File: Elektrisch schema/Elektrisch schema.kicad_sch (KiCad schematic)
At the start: 5 parts, among them J1 Conn_01x03_Socket, Q1 NPN

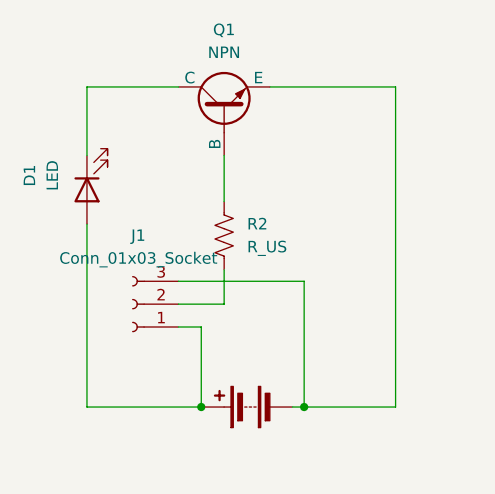
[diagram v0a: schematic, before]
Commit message: elektisch shema second draft
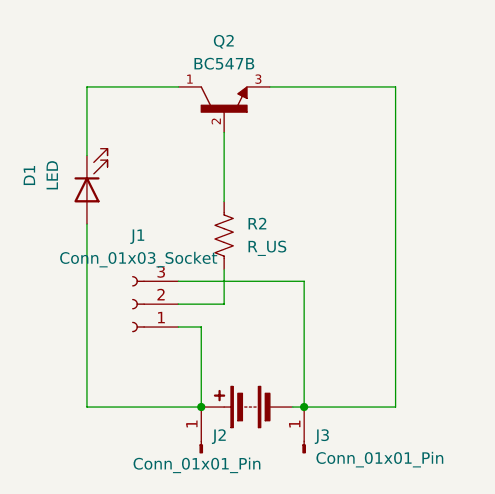
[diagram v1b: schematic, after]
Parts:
- removed Q1: NPN, symbol Simulation_SPICE:NPN
- added J2, J3: Conn_01x01_Pin, Connector_PinHeader_2.54mm:PinHeader_1x01_P2.54mm_Vertical, symbol Connector:Conn_01x01_Pin
- added Q2: BC547B, BC547B:TO92250P510H770-3, symbol BC547B:BC547B
- J1: footprint (none) -> Connector_PinHeader_2.54mm:PinHeader_1x03_P2.54mm_Vertical
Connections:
- net at D1.1 (K): now also Q2.1
- net at BT1.1 (+), D1.2 (A), J1.1 (Pin_1): now also J2.1 (Pin_1)
- net at BT1.2 (-), J1.3 (Pin_3): now also J3.1 (Pin_1), Q2.3
- net at R2.1: now also Q2.2
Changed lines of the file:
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@@
     (stroke (width 0) (type default))
   )
-  (wire (pts (xy 113.03 76.2) (xy 113.03 81.28))
+  (wire (pts (xy 113.03 73.66) (xy 113.03 81.28))
     (stroke (width 0) (type default))
   )
@@
     )
   )
+  (symbol (lib_id "BC547B:BC547B") (at 113.03 71.12 90) (unit 1)
+    (in_bom yes) (on_board yes) (dnp no) (fields_autoplaced)
+    (property "Reference" "Q2" (at 113.03 63.5 90)
+      (effects (font (size 1.27 1.27)))
+    )
+    (property "Value" "BC547B" (at 113.03 66.04 90)
+      (effects (font (size 1.27 1.27)))
+    )
+    (property "Footprint" "BC547B:TO92250P510H770-3" (at 113.03 71.12 0)
+      (effects (font (size 1.27 1.27)) (justify bottom) hide)
+    )
+    (property "Datasheet" "" (at 113.03 71.12 0)
+      (effects (font (size 1.27 1.27)) hide)
+    )
+    (property "MF" "onsemi" (at 113.03 71.12 0)
+      (effects (font (size 1.27 1.27)) (justify bottom) hide)
+    )
+    (property "Purchase-URL" "https://www.snapeda.com/api/url_track_click_mouser/?unipart_id=7207558&manufacturer=onsemi&part_name=BC547B&search_term=None" (at 113.03 71.12 0)
+      (effects (font (size 1.27 1.27)) (justify bottom) hide)
+    )
+    (property "Package" "E-PKG AXIAL-LEADED-2 ON Semiconductor" (at 113.03 71.12 0)
+      (effects (font (size 1.27 1.27)) (justify bottom) hide)
+    )
+    (property "Price" "None" (at 113.03 71.12 0)
+      (effects (font (size 1.27 1.27)) (justify bottom) hide)
+    )
+    (property "Check_prices" "https://www.snapeda.com/parts/BC547B/Onsemi/view-part/?ref=eda" (at 113.03 71.12 0)
+      (effects (font (size 1.27 1.27)) (justify bottom) hide)
+    )
+    (property "SnapEDA_Link" "https://www.snapeda.com/parts/BC547B/Onsemi/view-part/?ref=snap" (at 113.03 71.12 0)
+      (effects (font (size 1.27 1.27)) (justify bottom) hide)
+    )
+    (property "MP" "BC547B" (at 113.03 71.12 0)
+      (effects (font (size 1.27 1.27)) (justify bottom) hide)
+    )
+    (property "Availability" "In Stock" (at 113.03 71.12 0)
+      (effects (font (size 1.27 1.27)) (justify bottom) hide)
+    )
+    (property "Description" "\nBipolar (BJT) Transistor NPN 45 V 100 mA 300MHz 500 mW Through Hole TO-92-3\n" (at 113.03 71.12 0)
+      (effects (font (size 1.27 1.27)) (justify bottom) hide)
+    )
+    (pin "1")
+    (pin "2")
+    (pin "3")
+    (instances
+      (project "Elektrisch schema"
+        (path "/85b27cc0-7b51-4c2c-b0d4-ad8ed33695ec"
+          (reference "Q2") (unit 1)
+        )
+      )
+    )
+  )
   (symbol (lib_id "Device:Battery") (at 115.57 104.14 90) (unit 1)
     (in_bom yes) (on_board yes) (dnp no) (fields_autoplaced)
@@
     )
   )
-  (symbol (lib_id "Simulation_SPICE:NPN") (at 113.03 71.12 90) (unit 1)
+  (symbol (lib_id "Connector:Conn_01x01_Pin") (at 121.92 109.22 90) (unit 1)
     (in_bom yes) (on_board yes) (dnp no) (fields_autoplaced)
-    (property "Reference" "Q1" (at 113.03 62.23 90)
-      (effects (font (size 1.27 1.27)))
+    (property "Reference" "J3" (at 123.19 107.315 90)
+      (effects (font (size 1.27 1.27)) (justify right))
     )
-    (property "Value" "NPN" (at 113.03 64.77 90)
-      (effects (font (size 1.27 1.27)))
+    (property "Value" "Conn_01x01_Pin" (at 123.19 109.855 90)
+      (effects (font (size 1.27 1.27)) (justify right))
     )
-    (property "Footprint" "" (at 113.03 7.62 0)
+    (property "Footprint" "Connector_PinHeader_2.54mm:PinHeader_1x01_P2.54mm_Vertical" (at 121.92 109.22 0)
       (effects (font (size 1.27 1.27)) hide)
     )
-    (property "Datasheet" "~" (at 113.03 7.62 0)
-      (effects (font (size 1.27 1.27)) hide)
-    )
-    (property "Sim.Device" "NPN" (at 113.03 71.12 0)
-      (effects (font (size 1.27 1.27)) hide)
-    )
-    (property "Sim.Type" "GUMMELPOON" (at 113.03 71.12 0)
-      (effects (font (size 1.27 1.27)) hide)
-    )
-    (property "Sim.Pins" "1=C 2=B 3=E" (at 113.03 71.12 0)
+    (property "Datasheet" "~" (at 121.92 109.22 0)
       (effects (font (size 1.27 1.27)) hide)
     )
     (pin "1")
-    (pin "2")
-    (pin "3")
     (instances
       (project "Elektrisch schema"
         (path "/85b27cc0-7b51-4c2c-b0d4-ad8ed33695ec"
-          (reference "Q1") (unit 1)
+          (reference "J3") (unit 1)
+        )
+      )
+    )
+  )
+  (symbol (lib_id "Connector:Conn_01x01_Pin") (at 110.49 109.22 90) (unit 1)
+    (in_bom yes) (on_board yes) (dnp no)
+    (property "Reference" "J2" (at 111.76 107.315 90)
+      (effects (font (size 1.27 1.27)) (justify right))
+    )
+    (property "Value" "Conn_01x01_Pin" (at 102.87 110.49 90)
+      (effects (font (size 1.27 1.27)) (justify right))
+    )
+    (property "Footprint" "Connector_PinHeader_2.54mm:PinHeader_1x01_P2.54mm_Vertical" (at 110.49 109.22 0)
+      (effects (font (size 1.27 1.27)) hide)
+    )
+    (property "Datasheet" "~" (at 110.49 109.22 0)
+      (effects (font (size 1.27 1.27)) hide)
+    )
+    (pin "1")
+    (instances
+      (project "Elektrisch schema"
+        (path "/85b27cc0-7b51-4c2c-b0d4-ad8ed33695ec"
+          (reference "J2") (unit 1)
         )
       )
@@
       (effects (font (size 1.27 1.27)))
     )
-    (property "Footprint" "" (at 102.87 92.71 0)
+    (property "Footprint" "Connector_PinHeader_2.54mm:PinHeader_1x03_P2.54mm_Vertical" (at 102.87 92.71 0)
       (effects (font (size 1.27 1.27)) hide)
     )

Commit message: updating github
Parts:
- added D2: 1N4001, Diode_THT:D_DO-41_SOD81_P10.16mm_Horizontal, symbol Diode:1N4001
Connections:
- net at BT1.1 (+), D1.2 (A), J1.1 (Pin_1): now also D2.1 (K); no longer J2.1 (Pin_1)
- new net: D2.2 (A), J2.1 (Pin_1)
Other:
- moved on the sheet: J2
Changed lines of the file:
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@@
 (kicad_sch (version 20230121) (generator eeschema)
   (paper "A4")
+  (junction (at 110.49 104.14) (diameter 0) (color 0 0 0 0)
+  )
   (junction (at 121.92 104.14) (diameter 0) (color 0 0 0 0)
   )
-  (junction (at 110.49 104.14) (diameter 0) (color 0 0 0 0)
+  (junction (at 104.14 104.14) (diameter 0) (color 0 0 0 0)
   )
   (wire (pts (xy 121.92 90.17) (xy 121.92 104.14))
@@
     (stroke (width 0) (type default))
   )
-  (wire (pts (xy 110.49 104.14) (xy 97.79 104.14))
+  (wire (pts (xy 104.14 104.14) (xy 97.79 104.14))
     (stroke (width 0) (type default))
   )
@@
     (stroke (width 0) (type default))
   )
-  (wire (pts (xy 107.95 95.25) (xy 110.49 95.25))
+  (wire (pts (xy 104.14 95.25) (xy 107.95 95.25))
     (stroke (width 0) (type default))
   )
@@
     (stroke (width 0) (type default))
   )
-  (wire (pts (xy 110.49 95.25) (xy 110.49 104.14))
+  (wire (pts (xy 111.76 104.14) (xy 110.49 104.14))
+    (stroke (width 0) (type default))
+  )
+  (wire (pts (xy 104.14 95.25) (xy 104.14 104.14))
     (stroke (width 0) (type default))
   )
@@
   )
   (wire (pts (xy 121.92 104.14) (xy 132.08 104.14))
+    (stroke (width 0) (type default))
+  )
+  (wire (pts (xy 104.14 104.14) (xy 110.49 104.14))
+    (stroke (width 0) (type default))
+  )
+  (wire (pts (xy 111.76 106.68) (xy 111.76 104.14))
+    (stroke (width 0) (type default))
+  )
+  (wire (pts (xy 104.14 106.68) (xy 104.14 109.22))
     (stroke (width 0) (type default))
   )
@@
     )
   )
+  (symbol (lib_id "Diode:1N4001") (at 107.95 106.68 180) (unit 1)
+    (in_bom yes) (on_board yes) (dnp no) (fields_autoplaced)
+    (property "Reference" "D2" (at 107.95 113.03 0)
+      (effects (font (size 1.27 1.27)))
+    )
+    (property "Value" "1N4001" (at 107.95 110.49 0)
+      (effects (font (size 1.27 1.27)))
+    )
+    (property "Footprint" "Diode_THT:D_DO-41_SOD81_P10.16mm_Horizontal" (at 107.95 106.68 0)
+      (effects (font (size 1.27 1.27)) hide)
+    )
+    (property "Datasheet" "http://www.vishay.com/docs/88503/1n4001.pdf" (at 107.95 106.68 0)
+      (effects (font (size 1.27 1.27)) hide)
+    )
+    (property "Sim.Device" "D" (at 107.95 106.68 0)
+      (effects (font (size 1.27 1.27)) hide)
+    )
+    (property "Sim.Pins" "1=K 2=A" (at 107.95 106.68 0)
+      (effects (font (size 1.27 1.27)) hide)
+    )
+    (pin "1")
+    (pin "2")
+    (instances
+      (project "Elektrisch schema"
+        (path "/85b27cc0-7b51-4c2c-b0d4-ad8ed33695ec"
+          (reference "D2") (unit 1)
+        )
+      )
+    )
+  )
   (symbol (lib_id "Connector:Conn_01x01_Pin") (at 121.92 109.22 90) (unit 1)
     (in_bom yes) (on_board yes) (dnp no) (fields_autoplaced)
@@
     )
   )
-  (symbol (lib_id "Connector:Conn_01x01_Pin") (at 110.49 109.22 90) (unit 1)
+  (symbol (lib_id "Connector:Conn_01x01_Pin") (at 104.14 114.3 90) (unit 1)
     (in_bom yes) (on_board yes) (dnp no)
-    (property "Reference" "J2" (at 111.76 107.315 90)
-      (effects (font (size 1.27 1.27)) (justify right))
-    )
-    (property "Value" "Conn_01x01_Pin" (at 102.87 110.49 90)
-      (effects (font (size 1.27 1.27)) (justify right))
-    )
-    (property "Footprint" "Connector_PinHeader_2.54mm:PinHeader_1x01_P2.54mm_Vertical" (at 110.49 109.22 0)
-      (effects (font (size 1.27 1.27)) hide)
-    )
-    (property "Datasheet" "~" (at 110.49 109.22 0)
-      (effects (font (size 1.27 1.27)) hide)
-    )
+    (property "Reference" "J2" (at 105.41 112.395 90)
+      (effects (font (size 1.27 1.27)) (justify right))
+    )
+    (property "Value" "Conn_01x01_Pin" (at 96.52 115.57 90)
+      (effects (font (size 1.27 1.27)) (justify right))
+    )
+    (property "Footprint" "Connector_PinHeader_2.54mm:PinHeader_1x01_P2.54mm_Vertical" (at 104.14 114.3 0)
+      (effects (font (size 1.27 1.27)) hide)
+    )
+    (property "Datasheet" "~" (at 104.14 114.3 0)
+      (effects (font (size 1.27 1.27)) hide)
+    )

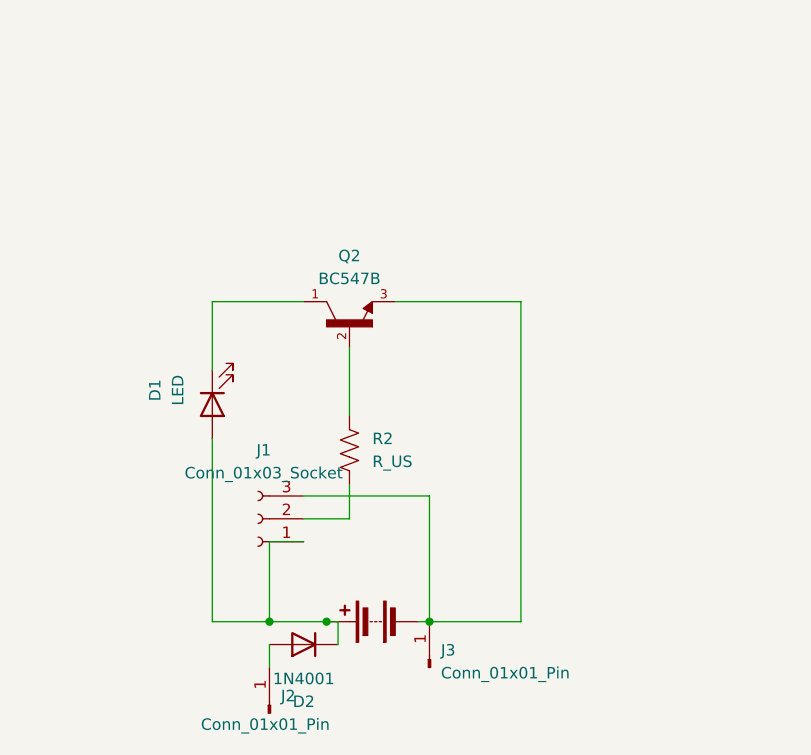
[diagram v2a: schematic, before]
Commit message: Readme bijgevuld en schema gemaakt
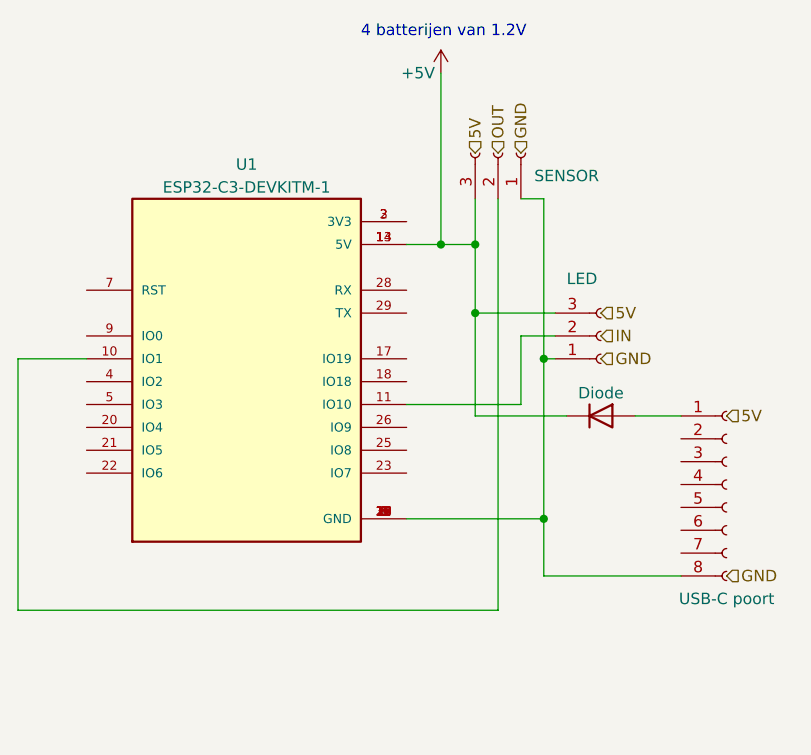
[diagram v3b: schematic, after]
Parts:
- removed BT1: Battery, Battery:BatteryHolder_Keystone_2462_2xAA, symbol Device:Battery
- removed D1: LED, LED_THT:LED_D5.0mm, symbol Device:LED
- removed D2: 1N4001, Diode_THT:D_DO-41_SOD81_P10.16mm_Horizontal, symbol Diode:1N4001
- removed J2, J3: Conn_01x01_Pin, Connector_PinHeader_2.54mm:PinHeader_1x01_P2.54mm_Vertical, symbol Connector:Conn_01x01_Pin
- removed Q2: BC547B, BC547B:TO92250P510H770-3, symbol BC547B:BC547B
- removed R2: R_US, Resistor_SMD:R_0805_2012Metric, symbol Device:R_US
- added D1: Diode, Diode_THT:D_DO-41_SOD81_P10.16mm_Horizontal, symbol Diode:BA157
- added J2: SENSOR, symbol Connector:Conn_01x03_Socket
- added J3: USB-C poort, symbol Connector:Conn_01x08_Socket
- added U1: ESP32-C3-DEVKITM-1, ESP32-C3-DEVKITM-1:XCVR_ESP32-C3-DEVKITM-1, symbol ESP32-C3-DEVKITM-1:ESP32-C3-DEVKITM-1
- J1: value Conn_01x03_Socket -> LED; footprint Connector_PinHeader_2.54mm:PinHeader_1x03_P2.54mm_Vertical -> (none)
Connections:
- net at J1.1 (Pin_1): now also J2.1 (Pin_1), J3.8 (Pin_8), U1.1 (GND), U1.12 (GND), U1.15 (GND), U1.16 (GND), U1.19 (GND), U1.24 (GND), U1.27 (GND), U1.30 (GND), U1.6 (GND), U1.8 (GND)
- net +5V: now reaches J1.3 (Pin_3)
- net +5V: now also D1.1 (K), J2.3 (Pin_3), U1.13 (5V), U1.14 (5V)
- net at J1.2 (Pin_2): now also U1.11 (IO10)
- new net: D1.2 (A), J3.1 (Pin_1)
- new net: J2.2 (Pin_2), U1.10 (IO1)
- new net: U1.2 (3V3), U1.3 (3V3)
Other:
- note added: "4 batterijen van 1.2V"
